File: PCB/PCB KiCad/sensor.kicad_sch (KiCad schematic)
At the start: 11 parts, among them U1 OPA2376xxD

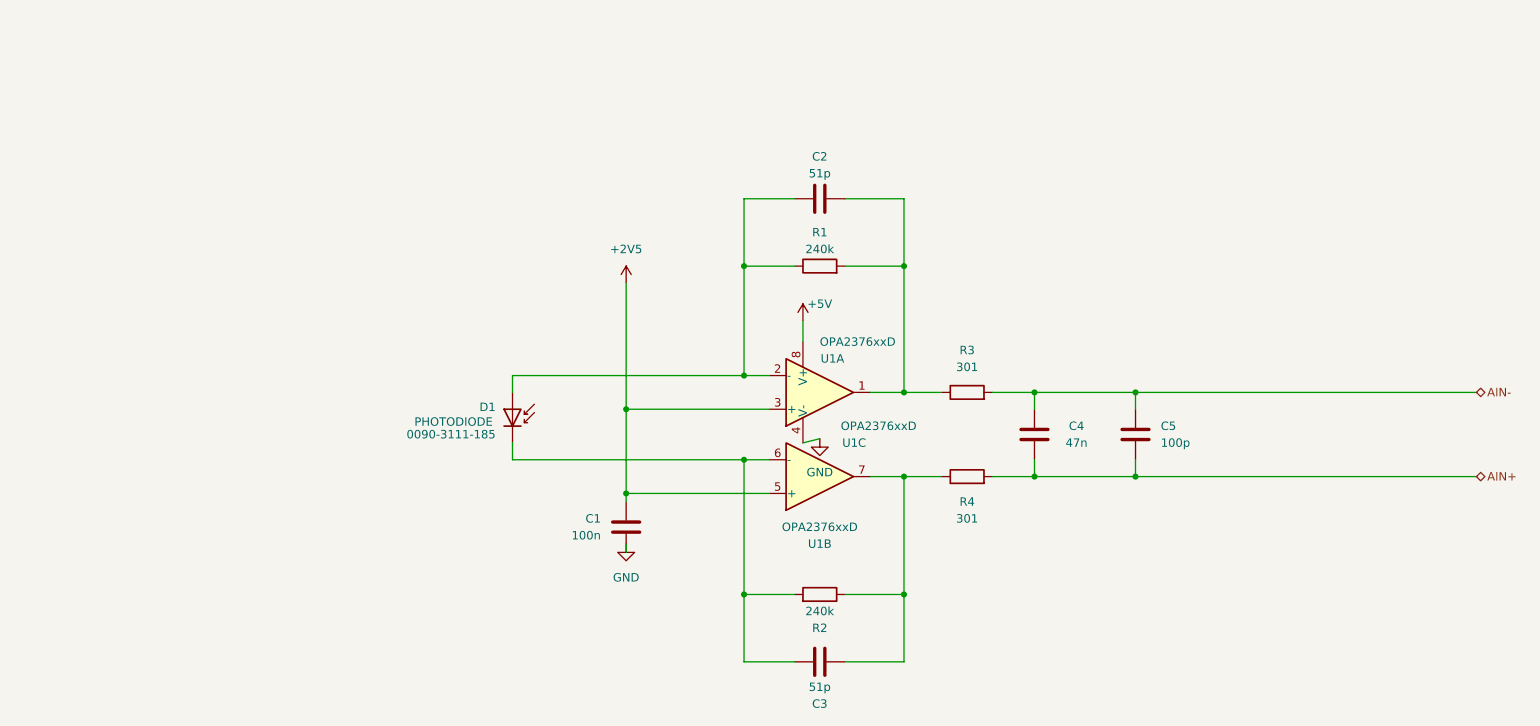
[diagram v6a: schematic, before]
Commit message: v2.2.0 first attempt for new ICs
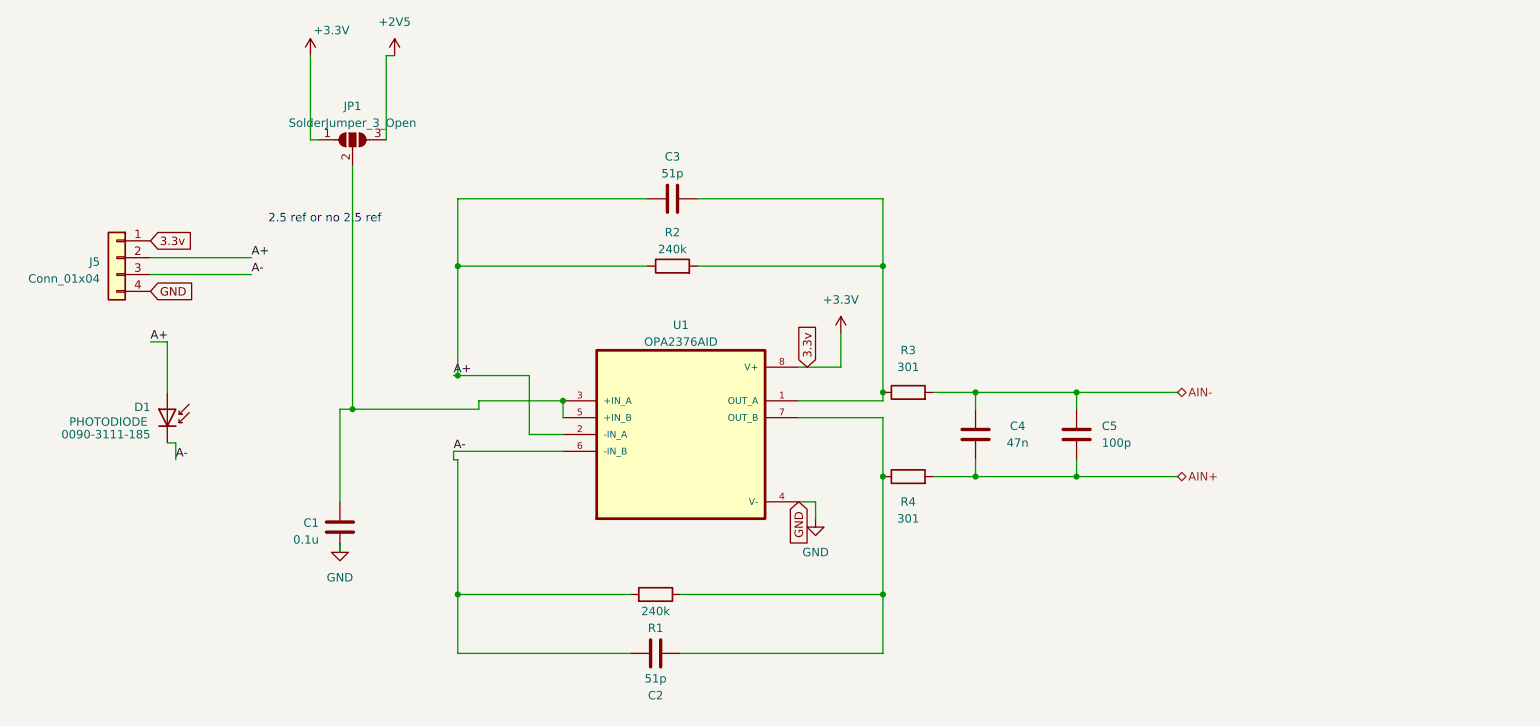
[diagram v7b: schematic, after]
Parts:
- removed U1: OPA2376xxD, eec:Texas_Instruments-OPA2376AID-Level_A, symbol Amplifier_Operational:OPA2376xxD
- added J5: Conn_01x04, Connector_PinSocket_2.54mm:PinSocket_1x04_P2.54mm_Vertical, symbol Connector_Generic:Conn_01x04
- added JP1: SolderJumper_3_Open, Jumper:SolderJumper-3_P2.0mm_Open_TrianglePad1.0x1.5mm, symbol Jumper:SolderJumper_3_Open
- added U1: OPA2376AID, OPA2376AID:SOIC127P599X175-8N, symbol OPA2376AID:OPA2376AID
- C1: value 100n -> 0.1u
- renumbered C3 to C2, C2 to C3, R2 to R1, R1 to R2
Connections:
- net +2V5: now also JP1.3 (B); no longer C1.2
- net GND: now also J5.4 (Pin_4), U1.4 (V-)
- net at C2.2, R1.1, R4.1: now also U1.7 (OUT_B)
- net A-: now reaches C2.1, D1.1 (K), R1.2
- net A-: now also J5.3 (Pin_3), U1.6 (-IN_B)
- net at C3.2, R2.2, R3.1: now also U1.1 (OUT_A)
- net A+: now reaches C3.1, D1.2 (A), R2.1
- net A+: now also J5.2 (Pin_2), U1.2 (-IN_A)
- new net: C1.2, JP1.2 (C), U1.3 (+IN_A), U1.5 (+IN_B)
- new net +3V3: J5.1 (Pin_1), JP1.1 (A), U1.8 (V+)
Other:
- note added: "2.5 ref or no 2.5 ref"
- moved on the sheet: C1, C2, C3, C4, C5, D1, R1, R2, R3, R4
